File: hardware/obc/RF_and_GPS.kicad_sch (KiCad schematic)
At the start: 10 parts, among them J5 SMA RA Connector, J6 SMA RA Connector, J7 SMA RA Connector, U14 S1216V8, U20 RFM9xBreakout, U23 RFM98PW

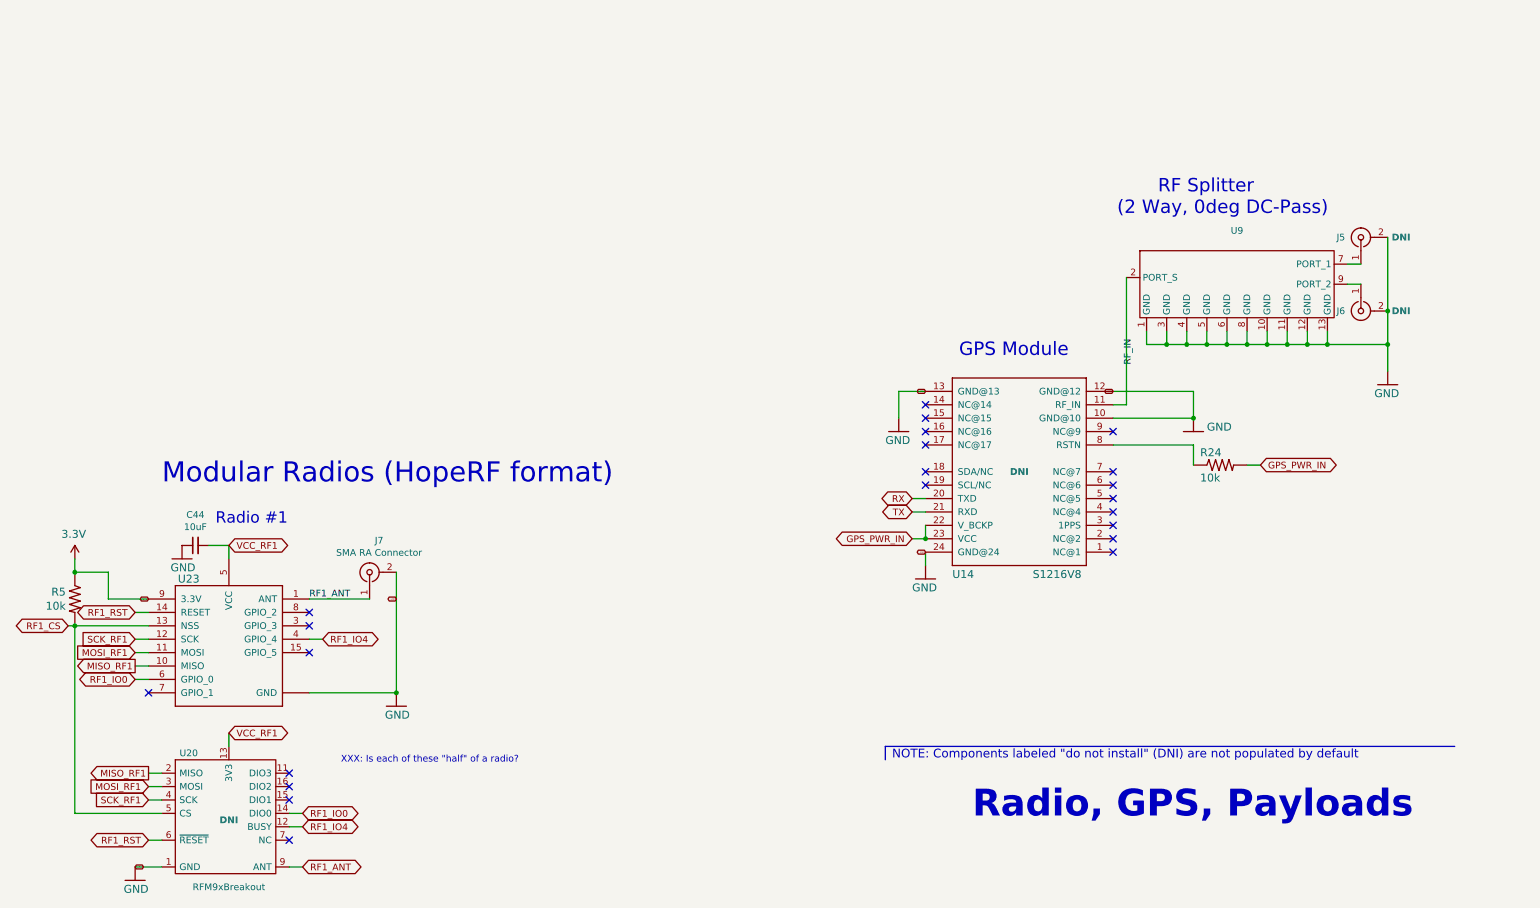
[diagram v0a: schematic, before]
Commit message: obc: Schematic pages to US Letter (except Power)
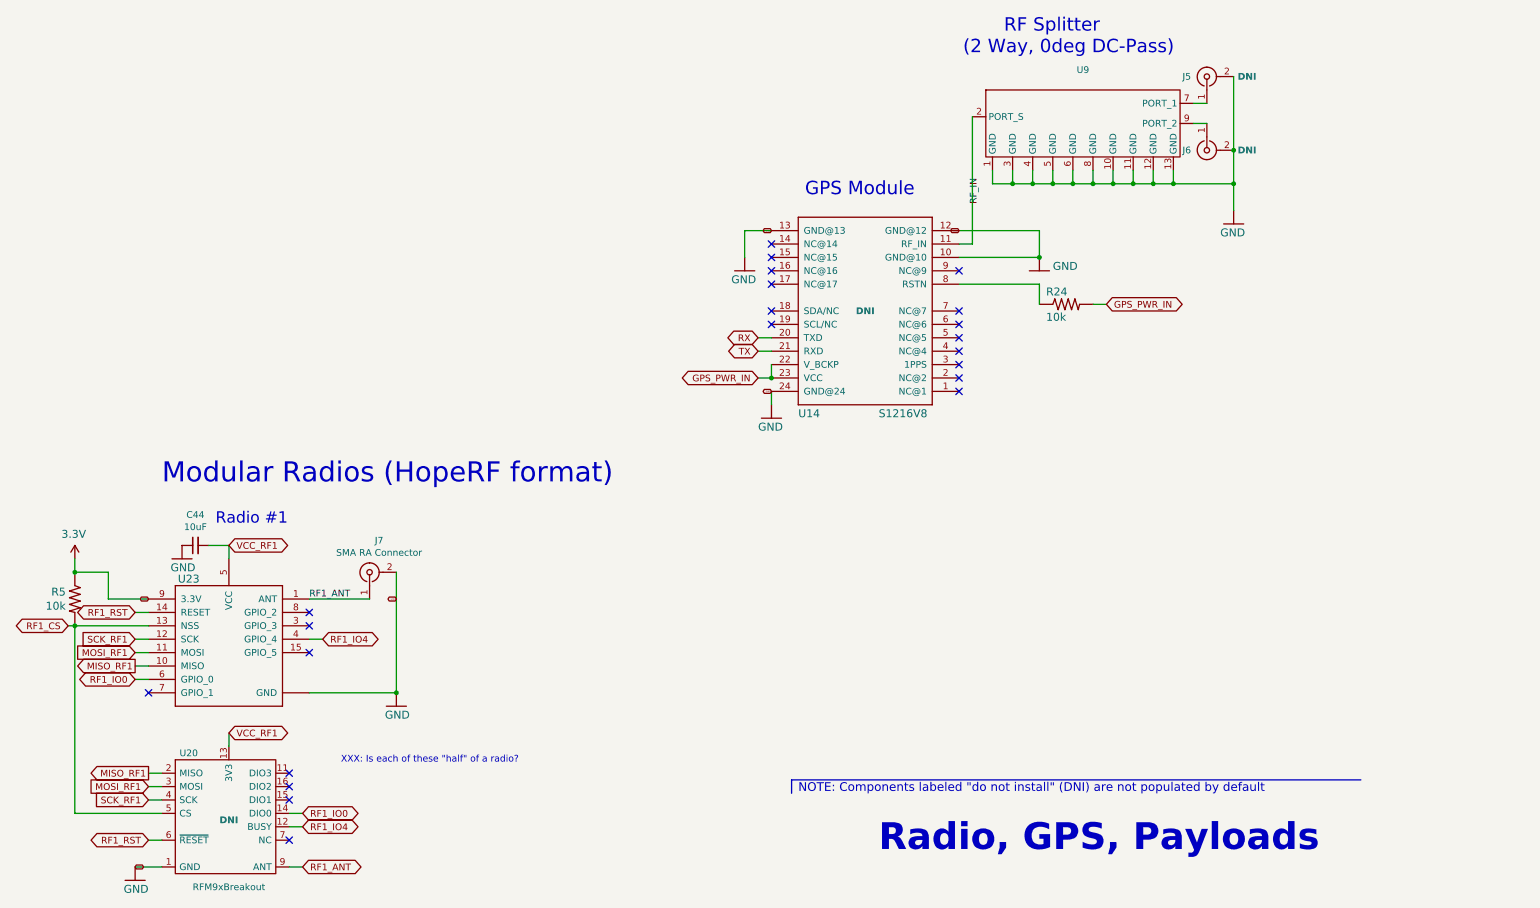
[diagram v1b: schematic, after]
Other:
- moved on the sheet: J5, J6, R24, U14, U9

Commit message: obc: schematic editing and footprint development
Deleted irrelevant SD-related circuits and pins. Created new & modified existing connector and inductor footprints. Added new components (Bat Charger, High-Rel Connector, etc.)
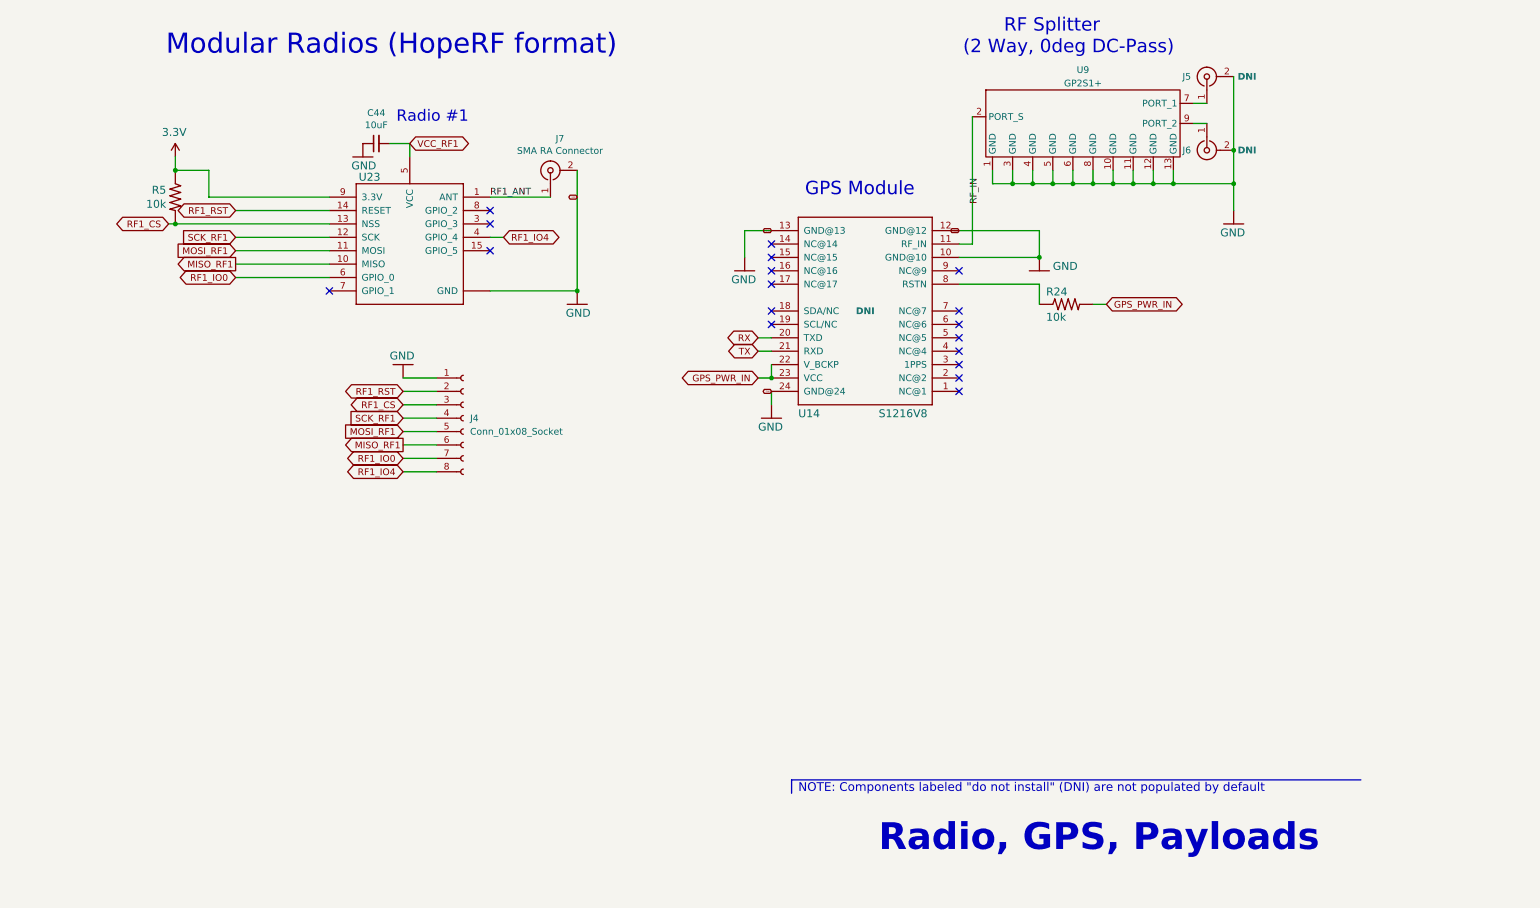
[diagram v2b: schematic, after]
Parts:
- removed U20: RFM9xBreakout, RF_Module:HOPERF_RFM9XW_SMD, symbol mainboard:RFM9xBreakout
- added J4: Conn_01x08_Socket, symbol Connector:Conn_01x08_Socket
- U14: Notes Necessary? -> Soldering ourselves
- U23: Notes (none) -> Soldering ourselves (other side of board)
- U9: value ~ -> GP2S1+; LCSC (none) -> C879828
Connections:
- net GND: now also J4.1 (Pin_1)
- net MISO_RF1: now also J4.6 (Pin_6)
- net MOSI_RF1: now also J4.5 (Pin_5)
- net RF1_CS: now also J4.3 (Pin_3)
- net RF1_IO0: now also J4.7 (Pin_7)
- net RF1_IO4: now also J4.8 (Pin_8)
- net RF1_RST: now also J4.2 (Pin_2)
- net SCK_RF1: now also J4.4 (Pin_4)
- no-connect marks 22 -> 18
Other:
- note removed: "XXX: Is each of these "half" of a radio?"
- moved on the sheet: C44, J7, R5, U23

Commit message: obc: BOM component verification
Verified part numbers, availability, values, footprints, etc. of components. Next steps involve verifying footprints and potentially researching some alternative components.
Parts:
- C44: Notes (none) -> 10V ok?
- J4: footprint (none) -> Connector_PinSocket_2.54mm:PinSocket_1x08_P2.54mm_Vertical; Notes (none) -> Not placed by JLCPCB
- J5, J6, J7: LCSC C429844/C3174972 -> (none); Notes Potential LCSC parts. Replace on schematic. -> Not placed by JLCPCB
- U14: Notes Soldering ourselves -> Not placed by JLCPCB
- U23: LCSC NotAvailable -> (none); Notes Soldering ourselves (other side of board) -> Not placed by JLCPCB (Soldering to back of board)
- U9: Manufacturer_Name (none) -> Mini Circuits; Manufacturer_Part_Number (none) -> GP2S1+

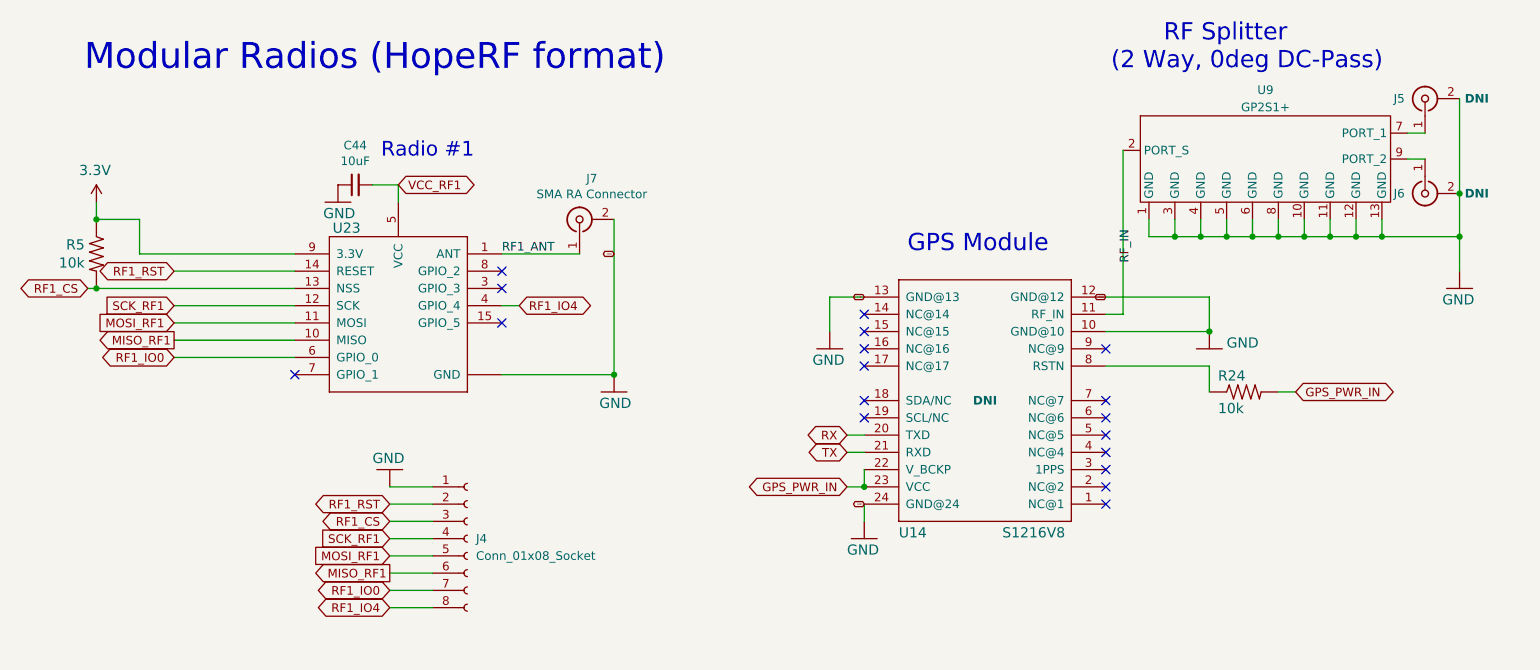
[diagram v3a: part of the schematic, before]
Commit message: obc: footprint editing and schematic revision
Added GPS21+ and edited inductor footprints. Edited schematic circuitry and re-annotated schematic components.
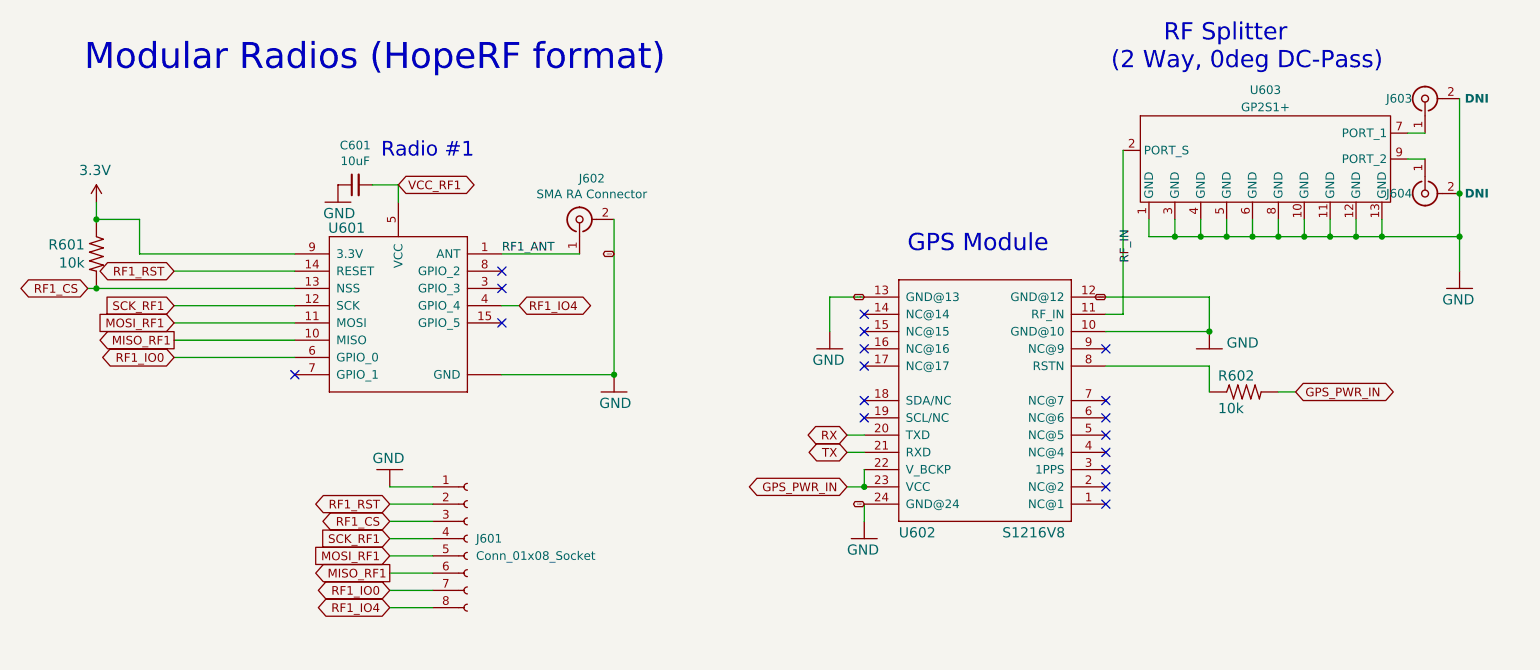
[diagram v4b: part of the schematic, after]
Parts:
- U602: renamed from U14; DNI DNI -> (none); Notes Not placed by JLCPCB -> (none)
- U603: renamed from U9; footprint (none) -> SSE_Footprints:DQ1225-12-1EP_3.0x3.0mm_P0.51mm
- renumbered C44 to C601, J4 to J601, J7 to J602, J5 to J603, J6 to J604, R5 to R601, R24 to R602, U23 to U601
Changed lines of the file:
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@@
 		(on_board yes)
 		(dnp no)
-		(property "Reference" "R24"
+		(property "Reference" "R602"
 			(at 207.01 77.2414 0)
 			(effects
@@
 			(project "mainboard"
 				(path "/e3ac22ea-6806-4807-a025-571315789c25/00000000-0000-0000-0000-00005cec6281"
-					(reference "R24")
+					(reference "R602")
 					(unit 1)
 				)
@@
 		(on_board yes)
 		(dnp no)
-		(property "Reference" "#GND044"
+		(property "Reference" "#GND0607"
 			(at 242.57 63.5 0)
 			(effects
@@
 			(project "mainboard"
 				(path "/e3ac22ea-6806-4807-a025-571315789c25/00000000-0000-0000-0000-00005cec6281"
-					(reference "#GND044")
+					(reference "#GND0607")
 					(unit 1)
 				)
@@
 		(on_board yes)
 		(dnp no)
-		(property "Reference" "J5"
+		(property "Reference" "J603"
 			(at 233.68 35.56 90)
 			(effects
@@
 			(project "mainboard"
 				(path "/e3ac22ea-6806-4807-a025-571315789c25/00000000-0000-0000-0000-00005cec6281"
-					(reference "J5")
+					(reference "J603")
 					(unit 1)
 				)
@@
 		(on_board yes)
 		(dnp no)
-		(property "Reference" "J6"
+		(property "Reference" "J604"
 			(at 233.68 49.53 90)
 			(effects
@@
 			(project "mainboard"
 				(path "/e3ac22ea-6806-4807-a025-571315789c25/00000000-0000-0000-0000-00005cec6281"
-					(reference "J6")
+					(reference "J604")
 					(unit 1)
 				)
@@
 		(on_board yes)
 		(dnp no)
-		(property "Reference" "J7"
+		(property "Reference" "J602"
 			(at 114.8334 47.3202 90)
 			(effects
@@
 			(project "mainboard"
 				(path "/e3ac22ea-6806-4807-a025-571315789c25/00000000-0000-0000-0000-00005cec6281"
-					(reference "J7")
+					(reference "J602")
 					(unit 1)
 				)
@@
 		(on_board yes)
 		(dnp no)
-		(property "Reference" "U23"
+		(property "Reference" "U601"
 			(at 78.74 54.61 0)
 			(effects
@@
 			(project "mainboard"
 				(path "/e3ac22ea-6806-4807-a025-571315789c25/00000000-0000-0000-0000-00005cec6281"
-					(reference "U23")
+					(reference "U601")
 					(unit 1)
 				)
@@
 		(on_board yes)
 		(dnp no)
-		(property "Reference" "#GND0103"
+		(property "Reference" "#GND0603"
 			(at 118.11 78.74 0)
 			(effects
@@
 			(project "mainboard"
 				(path "/e3ac22ea-6806-4807-a025-571315789c25/00000000-0000-0000-0000-00005cec6281"
-					(reference "#GND0103")
+					(reference "#GND0603")
 					(unit 1)
 				)
@@
 		(on_board yes)
 		(dnp no)
-		(property "Reference" "R5"
+		(property "Reference" "R601"
 			(at 40.1828 57.0738 90)
 			(effects
@@
 			(project "mainboard"
 				(path "/e3ac22ea-6806-4807-a025-571315789c25/00000000-0000-0000-0000-00005cec6281"
-					(reference "R5")
+					(reference "R601")
 					(unit 1)
 				)
@@
 		(on_board yes)
 		(dnp no)
-		(property "Reference" "#SUPPLY0109"
+		(property "Reference" "#SUPPLY0601"
 			(at 41.91 50.8 0)
 			(effects
@@
 			(project "mainboard"
 				(path "/e3ac22ea-6806-4807-a025-571315789c25/00000000-0000-0000-0000-00005cec6281"
-					(reference "#SUPPLY0109")
+					(reference "#SUPPLY0601")
 					(unit 1)
 				)
@@
 		(on_board yes)
 		(dnp no)
-		(property "Reference" "C44"
+		(property "Reference" "C601"
 			(at 80.01 42.4434 90)
 			(effects
@@
 			(project "mainboard"
 				(path "/e3ac22ea-6806-4807-a025-571315789c25/00000000-0000-0000-0000-00005cec6281"
-					(reference "C44")
+					(reference "C601")
 					(unit 1)
 				)
@@
 		(on_board yes)
 		(dnp no)
-		(property "Reference" "#GND036"
+		(property "Reference" "#GND0601"
 			(at 77.47 50.8 0)
 			(effects
@@
 			(project "mainboard"
 				(path "/e3ac22ea-6806-4807-a025-571315789c25/00000000-0000-0000-0000-00005cec6281"
-					(reference "#GND036")
+					(reference "#GND0601")
 					(unit 1)
 				)
@@
 		(on_board yes)
 		(dnp no)
-		(property "Reference" "#GND042"
+		(property "Reference" "#GND0604"
 			(at 149.86 72.39 0)
 			(effects
@@
 			(project "mainboard"
 				(path "/e3ac22ea-6806-4807-a025-571315789c25/00000000-0000-0000-0000-00005cec6281"
-					(reference "#GND042")
+					(reference "#GND0604")
 					(unit 1)
 				)
@@
 		(on_board yes)
 		(dnp no)
-		(property "Reference" "#GND043"
+		(property "Reference" "#GND0605"
 			(at 154.94 100.33 0)
 			(effects
@@
 			(project "mainboard"
 				(path "/e3ac22ea-6806-4807-a025-571315789c25/00000000-0000-0000-0000-00005cec6281"
-					(reference "#GND043")
+					(reference "#GND0605")
 					(unit 1)
 				)
@@
 		(on_board yes)
 		(dnp no)
-		(property "Reference" "#GND047"
+		(property "Reference" "#GND0606"
 			(at 205.74 72.39 0)
 			(effects
@@
 			(project "mainboard"
 				(path "/e3ac22ea-6806-4807-a025-571315789c25/00000000-0000-0000-0000-00005cec6281"
-					(reference "#GND047")
+					(reference "#GND0606")
 					(unit 1)
 				)
@@
 		(on_board yes)
 		(dnp no)
-		(property "Reference" "U14"
+		(property "Reference" "U602"
 			(at 160.02 100.33 0)
 			(effects
@@
 			)
 		)
-		(property "DNI" "DNI"
+		(property "DNI" ""
 			(at 172.72 80.01 0)
 			(effects
@@
 			)
 		)
-		(property "Notes" "Not placed by JLCPCB"
+		(property "Notes" ""
 			(at 172.72 80.01 0)
 			(effects
@@
 			(project "mainboard"
 				(path "/e3ac22ea-6806-4807-a025-571315789c25/00000000-0000-0000-0000-00005cec6281"
-					(reference "U14")
+					(reference "U602")
 					(unit 1)
 				)
@@
 		(dnp no)
 		(fields_autoplaced yes)
-		(property "Reference" "U9"
+		(property "Reference" "U603"
 			(at 213.995 34.29 0)
 			(effects
@@
 			)
 		)
-		(property "Footprint" ""
+		(property "Footprint" "SSE_Footprints:DQ1225-12-1EP_3.0x3.0mm_P0.51mm"
 			(at 213.36 35.56 0)
 			(effects
@@
 			(project "mainboard"
 				(path "/e3ac22ea-6806-4807-a025-571315789c25/00000000-0000-0000-0000-00005cec6281"
-					(reference "U9")
+					(reference "U603")
 					(unit 1)
 				)
@@
 		(dnp no)
 		(fields_autoplaced yes)
-		(property "Reference" "J4"
+		(property "Reference" "J601"
 			(at 97.79 100.3299 0)
 			(effects
@@
 			(project "mainboard"
 				(path "/e3ac22ea-6806-4807-a025-571315789c25/00000000-0000-0000-0000-00005cec6281"
-					(reference "J4")
+					(reference "J601")
 					(unit 1)
 				)
@@
 		(on_board yes)
 		(dnp no)
-		(property "Reference" "#GND033"
+		(property "Reference" "#GND0602"
 			(at 85.09 90.17 0)
 			(effects
@@
 			(project "mainboard"
 				(path "/e3ac22ea-6806-4807-a025-571315789c25/00000000-0000-0000-0000-00005cec6281"
-					(reference "#GND033")
+					(reference "#GND0602")
 					(unit 1)
 				)
